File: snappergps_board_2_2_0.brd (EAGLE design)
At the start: 26.3 x 32 mm, 66 parts, among them IC1 W25N512GVEIG_W25N512GVEIG, J1 DX07S016JA1R1500, J4 2988, J5 2988, Q1 TT8M1TRAMANDA, Q3 TT8M1TRAMANDA, Q4 TT8M1TRAMANDA, U1 EFM32HG310F64, U2 RF_CIRCUIT-SE4150L, U3 TVS_DIODE-PRTR5V0U2AX, U6 TPS61291DRVT, U7 MDMK2020T3R3MM

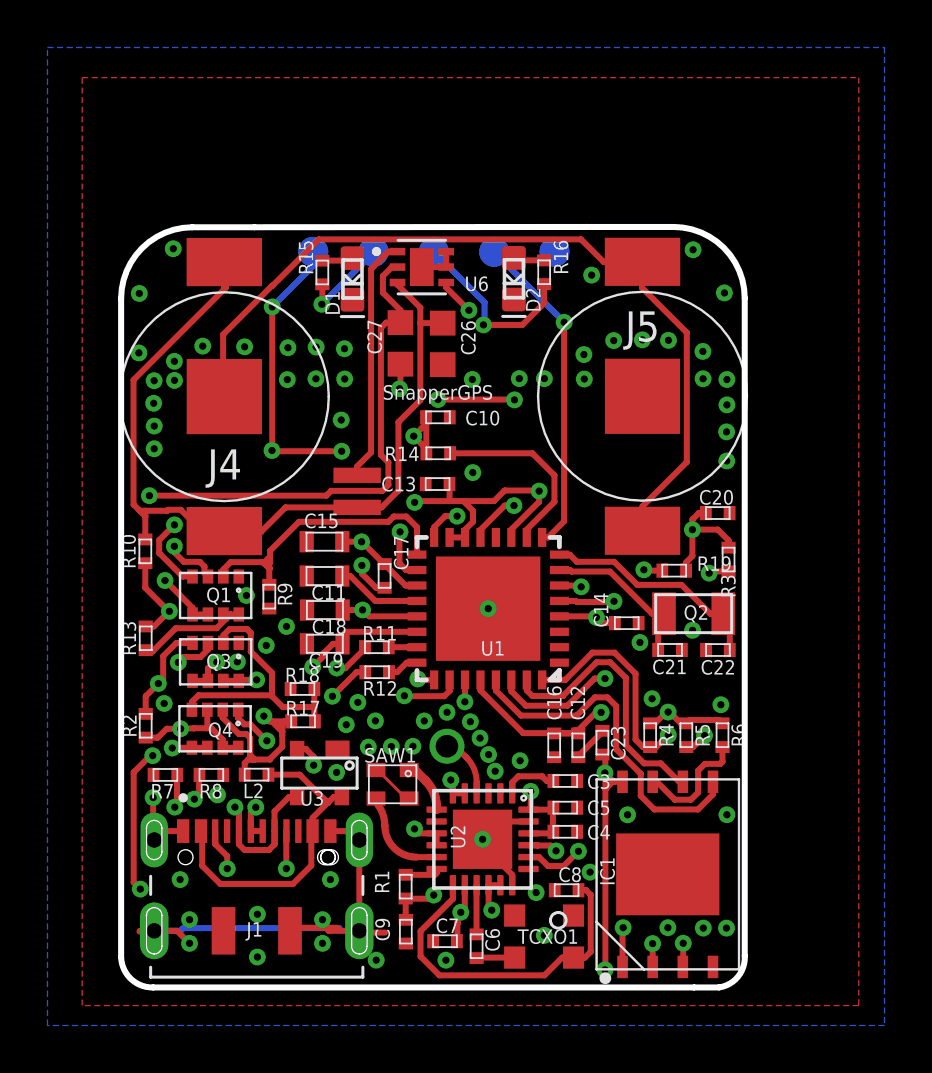
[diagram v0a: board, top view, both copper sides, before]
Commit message: Replace coin cells with lipo, add lipo charger
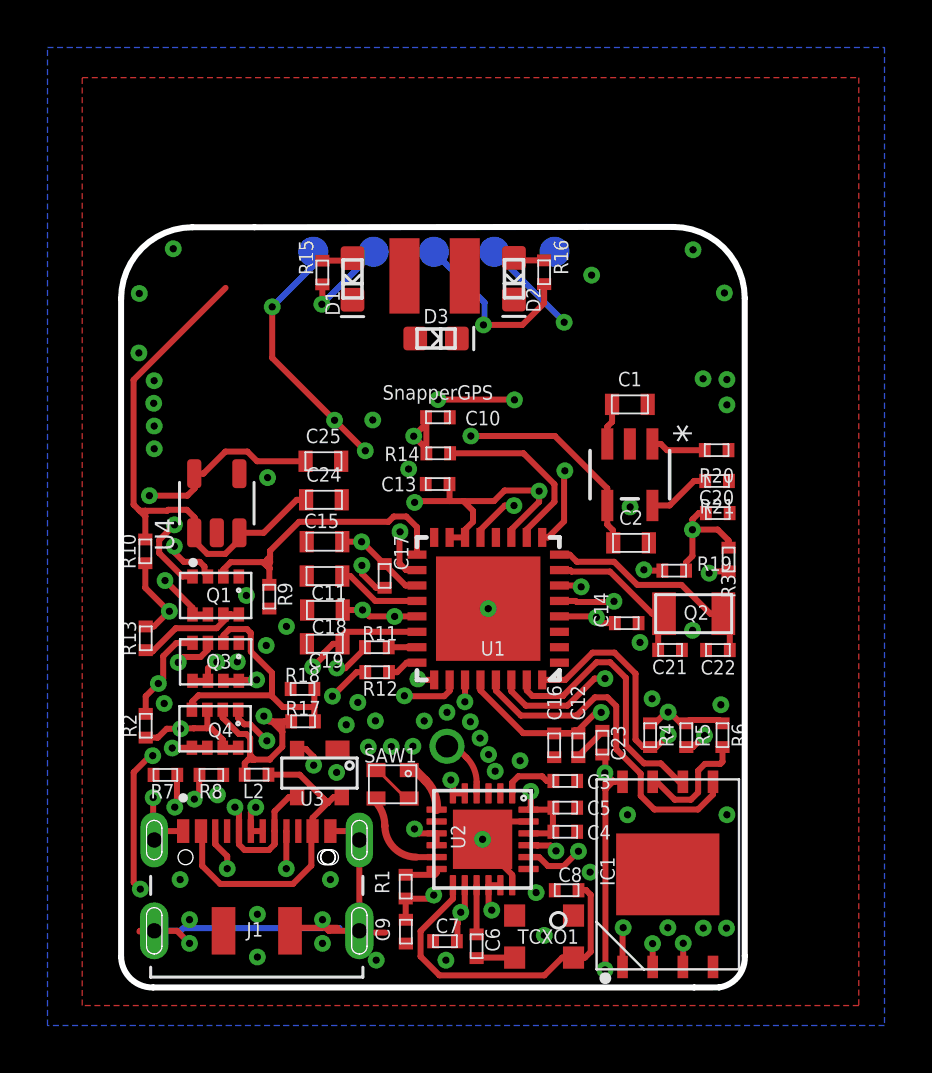
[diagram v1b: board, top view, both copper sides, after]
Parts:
- removed C26: 10uF, rcl:C0603K
- removed C27: 22uF, rcl:C0603K
- removed J4, J5: 2988, 2988:2988
- removed U6: TPS61291DRVT, TPS61291DRVT:SON65P200X200X80-7N
- removed U7: MDMK2020T3R3MM, alex:MDMK2020T3R3MM
- added C1, C2: 4.7uF, bird_variant_2:0603
- added C24, C25: 1uF, bird_variant_2:0603
- added D3: (no value), bird_variant_2:LED-0603
- added R20: 1K, bird_variant_2:0402
- added R21: 25K, bird_variant_2:0402
- added U$3: INDUCTION_BOARD_CONN2, inductive_sensor_daughterboard:INDUCTION_BOARD_CONN2
- added U4: S-1318D33-M5T1U4, SOT95P280X145-5N-volt:SOT95P280X145-5N
- added U5: MCP73831T-2ACI/OT, mcp73831T-2ACI:SOT-23-5_MC_MCH
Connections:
- removed net N$20: J4.2, J5.1, J5.3
- new net N$15: R20.2, U5.1
- new net N$21: R21.2, U5.5
- net 3V3: now also C25.1, U4.5; no longer C27.1, U6.2
- net DC_BOOST_EN: no longer U6.4
- net GND: now also C1.2, C2.2, C24.2, C25.2, R21.1, U$3.P$2, U4.2, U4.4, U5.2; no longer C26.2, C27.2, J5.2, U6.5, U6.6, U6.7
- net N$7: now also D3.C, R20.1; no longer U6.1, U7.P$2
- net VBAT: now also C1.1, C24.1, U$3.P$1, U4.1, U4.3, U5.3; no longer C26.1, J4.1, J4.3, U6.3, U7.P$1
- net VBUS: now also C2.1, D3.A, U5.4
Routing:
- net N$20: track 35.2 -> 0.00 mm
- net VBUS: track 18.6 -> 37.8 mm, vias 2 -> 4
- net VBAT: track 38.1 -> 24.0 mm
- net 3V3: track 33.7 -> 20.6 mm
- net DC_BOOST_EN: track 12.0 -> 0.00 mm, vias 2 -> 0
- net N$7: track 10.3 -> 0.00 mm
- net GND: track 37.7 -> 34.8 mm, vias 83 -> 63
- net N$21: track 0.00 -> 2.65 mm
- net N$15: track 0.00 -> 2.32 mm
- net VDD: track 92.3 -> 93.7 mm
- net N$2: track 34.6 -> 35.7 mm
- net RESET: vias 1 -> 2

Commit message: Update board layout
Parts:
- moved D3 11.6 mm to (26.0, 24.5)
- moved D1 3.50 mm to (11.2, 26.3)
- moved D2 3.50 mm to (18.0, 26.4)
- moved GND 3.50 mm to (19.7, 27.5)
- moved R15 3.50 mm to (9.96, 26.6)
- moved R16 3.50 mm to (19.3, 26.6)
- moved RESET 3.50 mm to (17.2, 27.5)
- moved SWCLK 3.50 mm to (14.7, 27.5)
- moved SWDIO 3.50 mm to (12.1, 27.5)
- moved U$3 3.50 mm to (14.7, 26.5)
- moved VDD 3.50 mm to (9.58, 27.5)
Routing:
- net VBAT: track 24.0 -> 39.6 mm, vias 0 -> 2
- net VBUS: track 37.8 -> 44.7 mm
- net VDD: track 93.7 -> 89.2 mm
- net SWDIO/GREEN: track 32.5 -> 28.7 mm
- net RESET: track 13.8 -> 10.3 mm
- net SWCLK/RED: track 24.7 -> 21.8 mm
- net N$7: track 0.00 -> 1.96 mm
- net N$14: track 25.0 -> 23.5 mm
- net GND: vias 63 -> 79
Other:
- board size 26.3 x 32 mm -> 26.3 x 28.5 mm

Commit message: Add manufacturing files & tweak PCB
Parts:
- renumbered C1 to C101, C2 to C102, C24 to C124, C25 to C125, D3 to D103, R20 to R120, R21 to R121, U4 to U104, U5 to U105
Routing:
- net GND: vias 79 -> 80
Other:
- outline, holes or cut-outs redrawn
- board text added: "V2.2.0-LiPo"
- board text removed: "V2.2.0"
